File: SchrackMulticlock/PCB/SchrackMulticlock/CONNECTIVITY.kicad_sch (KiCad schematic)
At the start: 24 parts, among them J1 TYPE-C-31-M-12 (USB C CONN), U7 USBLC6-2SC6

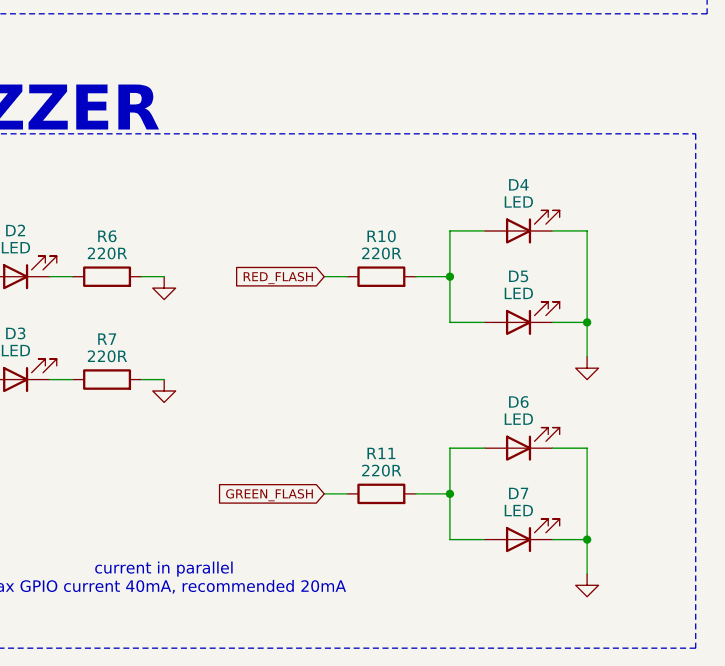
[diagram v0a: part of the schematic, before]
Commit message: Stopwatch.h + Schematic update
Multiclock Scheamtic and code update
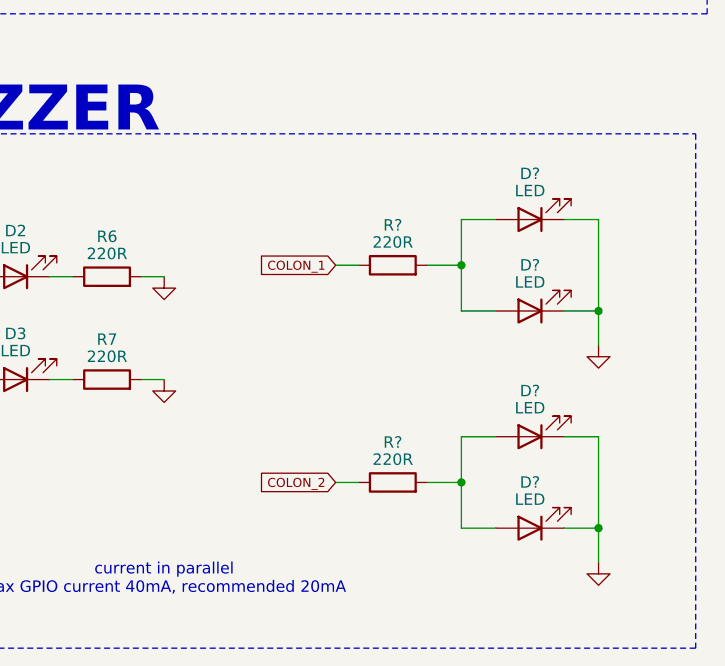
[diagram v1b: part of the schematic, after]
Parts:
- removed D4, D5, D6, D7: LED, LED_SMD:LED_0805_2012Metric_Pad1.15x1.40mm_HandSolder, symbol Device:LED
- removed R10, R11: 220R, Resistor_SMD:R_0805_2012Metric_Pad1.20x1.40mm_HandSolder, symbol Device:R
- added D? (x4): LED, LED_SMD:LED_0805_2012Metric_Pad1.15x1.40mm_HandSolder, symbol Device:LED
- added R? (x2): 220R, Resistor_SMD:R_0805_2012Metric_Pad1.20x1.40mm_HandSolder, symbol Device:R
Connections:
- net GND: now also D?.1 (K), D?.1 (K), D?.1 (K), D?.1 (K)
- new net: D?.2 (A), D?.2 (A), R?.2 (x2)
- new net COLON_1: R?.1
- new net COLON_2: R?.1

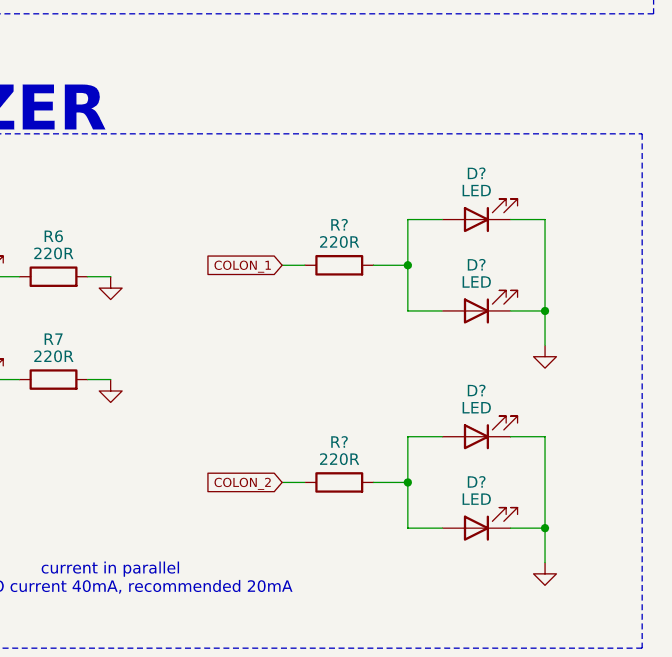
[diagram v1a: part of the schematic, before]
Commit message: SchrackMulticlock and Counter update
Schematic update for both
PCB update for Counter
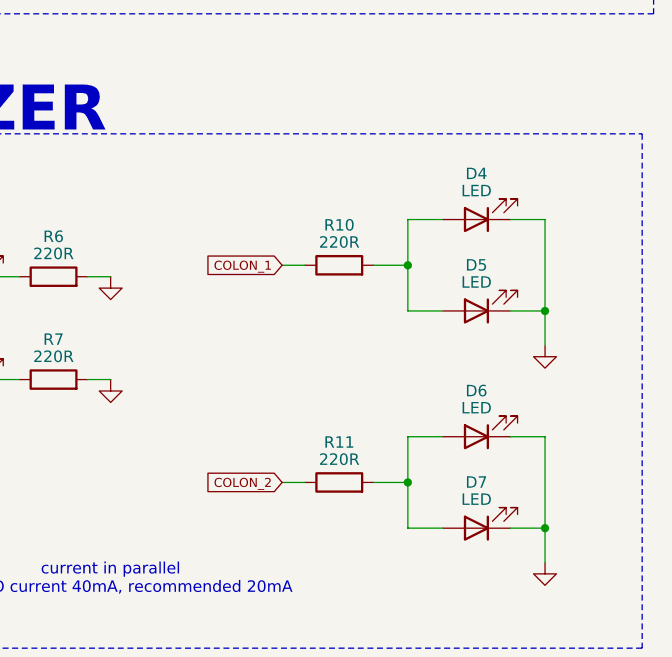
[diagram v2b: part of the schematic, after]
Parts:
- D4: renamed from D?; footprint LED_SMD:LED_0805_2012Metric_Pad1.15x1.40mm_HandSolder -> LED_SMD:LED_Cree-PLCC4_3.2x2.8mm_CCW
- gave numbers to parts that had none: 5
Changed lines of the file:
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@@
 		(on_board yes)
 		(dnp no)
-		(property "Reference" "D?"
+		(property "Reference" "D5"
 			(at 217.17 116.84 0)
 			(effects
@@
 			(project "SchrackMulticlock"
 				(path "/d96f2ffc-3f4c-4f71-b693-29f6b8c3245d/301b3ab9-8372-40d2-93c7-cd7607d23fc4"
-					(reference "D?")
+					(reference "D5")
 					(unit 1)
 				)
@@
 		(on_board yes)
 		(dnp no)
-		(property "Reference" "D?"
+		(property "Reference" "D6"
 			(at 217.17 130.81 0)
 			(effects
@@
 			(project "SchrackMulticlock"
 				(path "/d96f2ffc-3f4c-4f71-b693-29f6b8c3245d/301b3ab9-8372-40d2-93c7-cd7607d23fc4"
-					(reference "D?")
+					(reference "D6")
 					(unit 1)
 				)
@@
 		(dnp no)
 		(fields_autoplaced yes)
-		(property "Reference" "#PWR041"
+		(property "Reference" "#PWR023"
 			(at 224.79 132.08 0)
 			(effects
@@
 			(project "SchrackMulticlock"
 				(path "/d96f2ffc-3f4c-4f71-b693-29f6b8c3245d/301b3ab9-8372-40d2-93c7-cd7607d23fc4"
-					(reference "#PWR041")
+					(reference "#PWR023")
 					(unit 1)
 				)
@@
 		(dnp no)
 		(fields_autoplaced yes)
-		(property "Reference" "#PWR042"
+		(property "Reference" "#PWR024"
 			(at 224.79 156.21 0)
 			(effects
@@
 			(project "SchrackMulticlock"
 				(path "/d96f2ffc-3f4c-4f71-b693-29f6b8c3245d/301b3ab9-8372-40d2-93c7-cd7607d23fc4"
-					(reference "#PWR042")
+					(reference "#PWR024")
 					(unit 1)
 				)
@@
 		(on_board yes)
 		(dnp no)
-		(property "Reference" "R?"
+		(property "Reference" "R11"
 			(at 201.93 136.525 90)
 			(effects
@@
 			(project "SchrackMulticlock"
 				(path "/d96f2ffc-3f4c-4f71-b693-29f6b8c3245d/301b3ab9-8372-40d2-93c7-cd7607d23fc4"
-					(reference "R?")
+					(reference "R11")
 					(unit 1)
 				)
@@
 		(on_board yes)
 		(dnp no)
-		(property "Reference" "D?"
+		(property "Reference" "D7"
 			(at 217.17 140.97 0)
 			(effects
@@
 			(project "SchrackMulticlock"
 				(path "/d96f2ffc-3f4c-4f71-b693-29f6b8c3245d/301b3ab9-8372-40d2-93c7-cd7607d23fc4"
-					(reference "D?")
+					(reference "D7")
 					(unit 1)
 				)
@@
 		(on_board yes)
 		(dnp no)
-		(property "Reference" "R?"
+		(property "Reference" "R10"
 			(at 201.93 112.395 90)
 			(effects
@@
 			(project "SchrackMulticlock"
 				(path "/d96f2ffc-3f4c-4f71-b693-29f6b8c3245d/301b3ab9-8372-40d2-93c7-cd7607d23fc4"
-					(reference "R?")
+					(reference "R10")
 					(unit 1)
 				)
@@
 		(on_board yes)
 		(dnp no)
-		(property "Reference" "D?"
+		(property "Reference" "D4"
 			(at 217.17 106.68 0)
 			(effects
@@
 			)
 		)
-		(property "Footprint" "LED_SMD:LED_0805_2012Metric_Pad1.15x1.40mm_HandSolder"
+		(property "Footprint" "LED_SMD:LED_Cree-PLCC4_3.2x2.8mm_CCW"
 			(at 217.17 111.76 0)
 			(effects
@@
 			(project "SchrackMulticlock"
 				(path "/d96f2ffc-3f4c-4f71-b693-29f6b8c3245d/301b3ab9-8372-40d2-93c7-cd7607d23fc4"
-					(reference "D?")
-					(unit 1)
-				)
+					(reference "D4")
+					(unit 1)
+				)

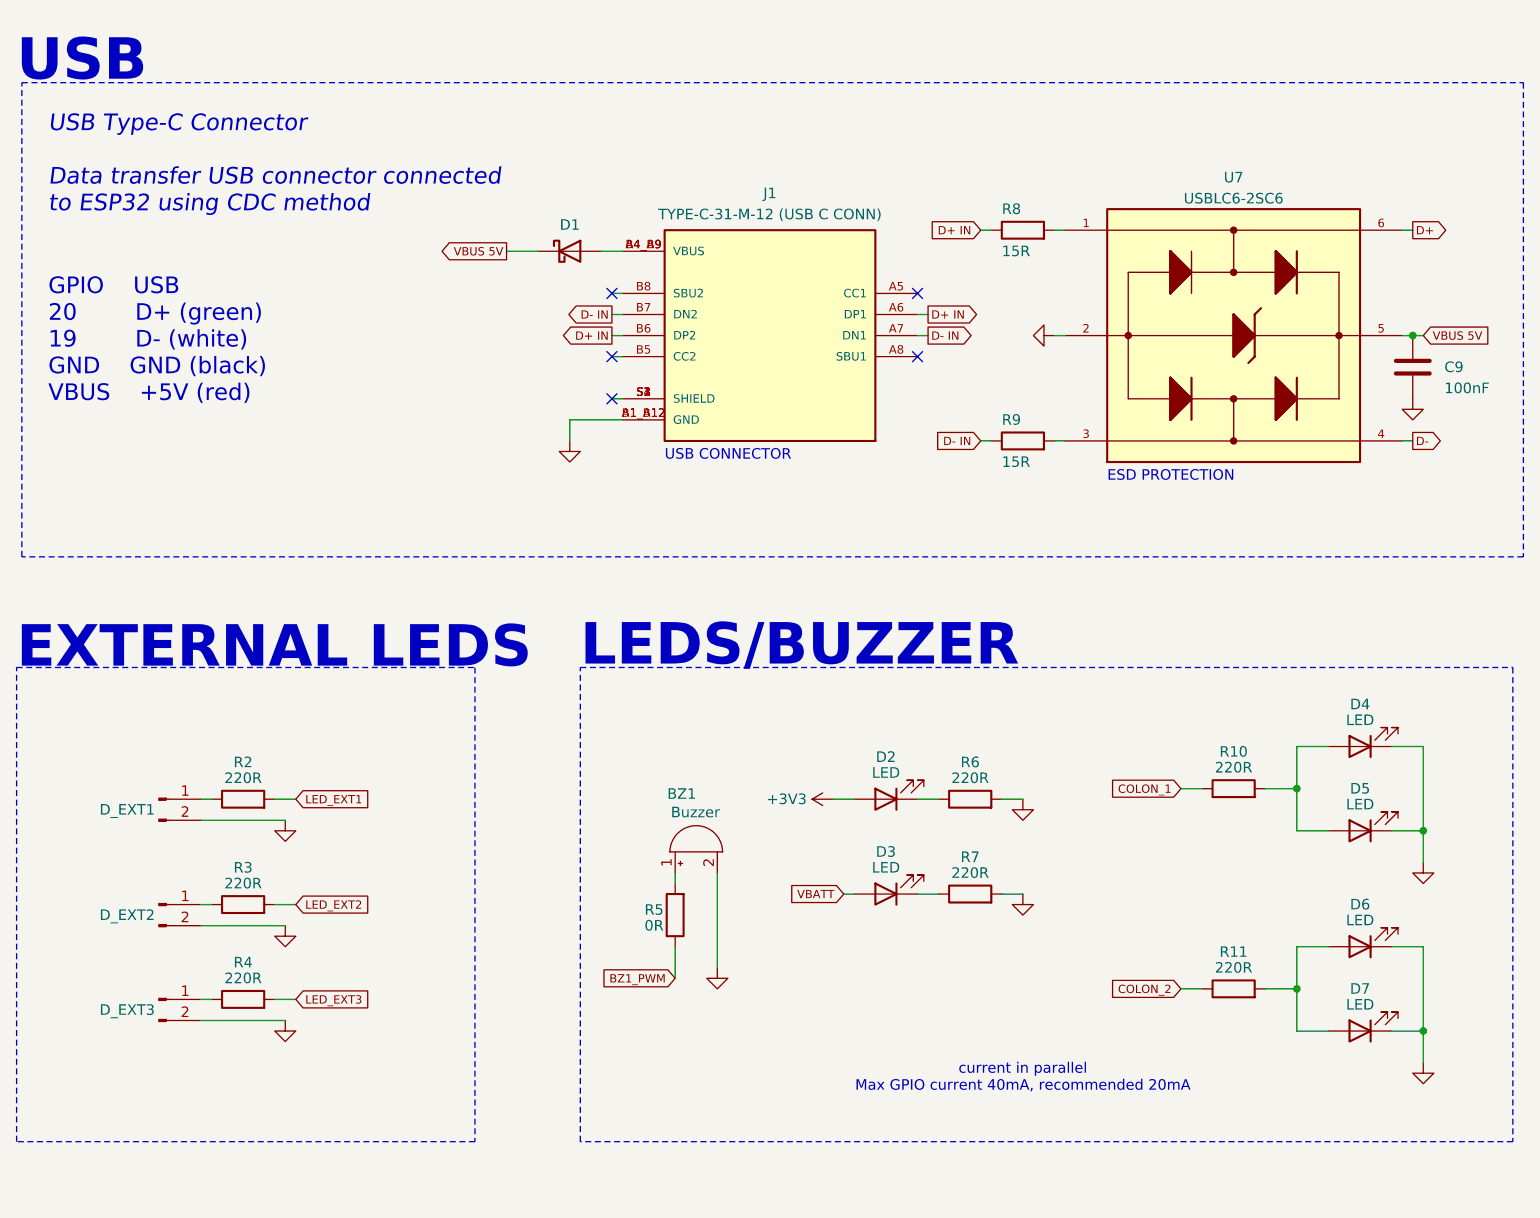
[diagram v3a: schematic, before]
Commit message: Schrackcounter Prototype update
Schematic + PCB update, final version
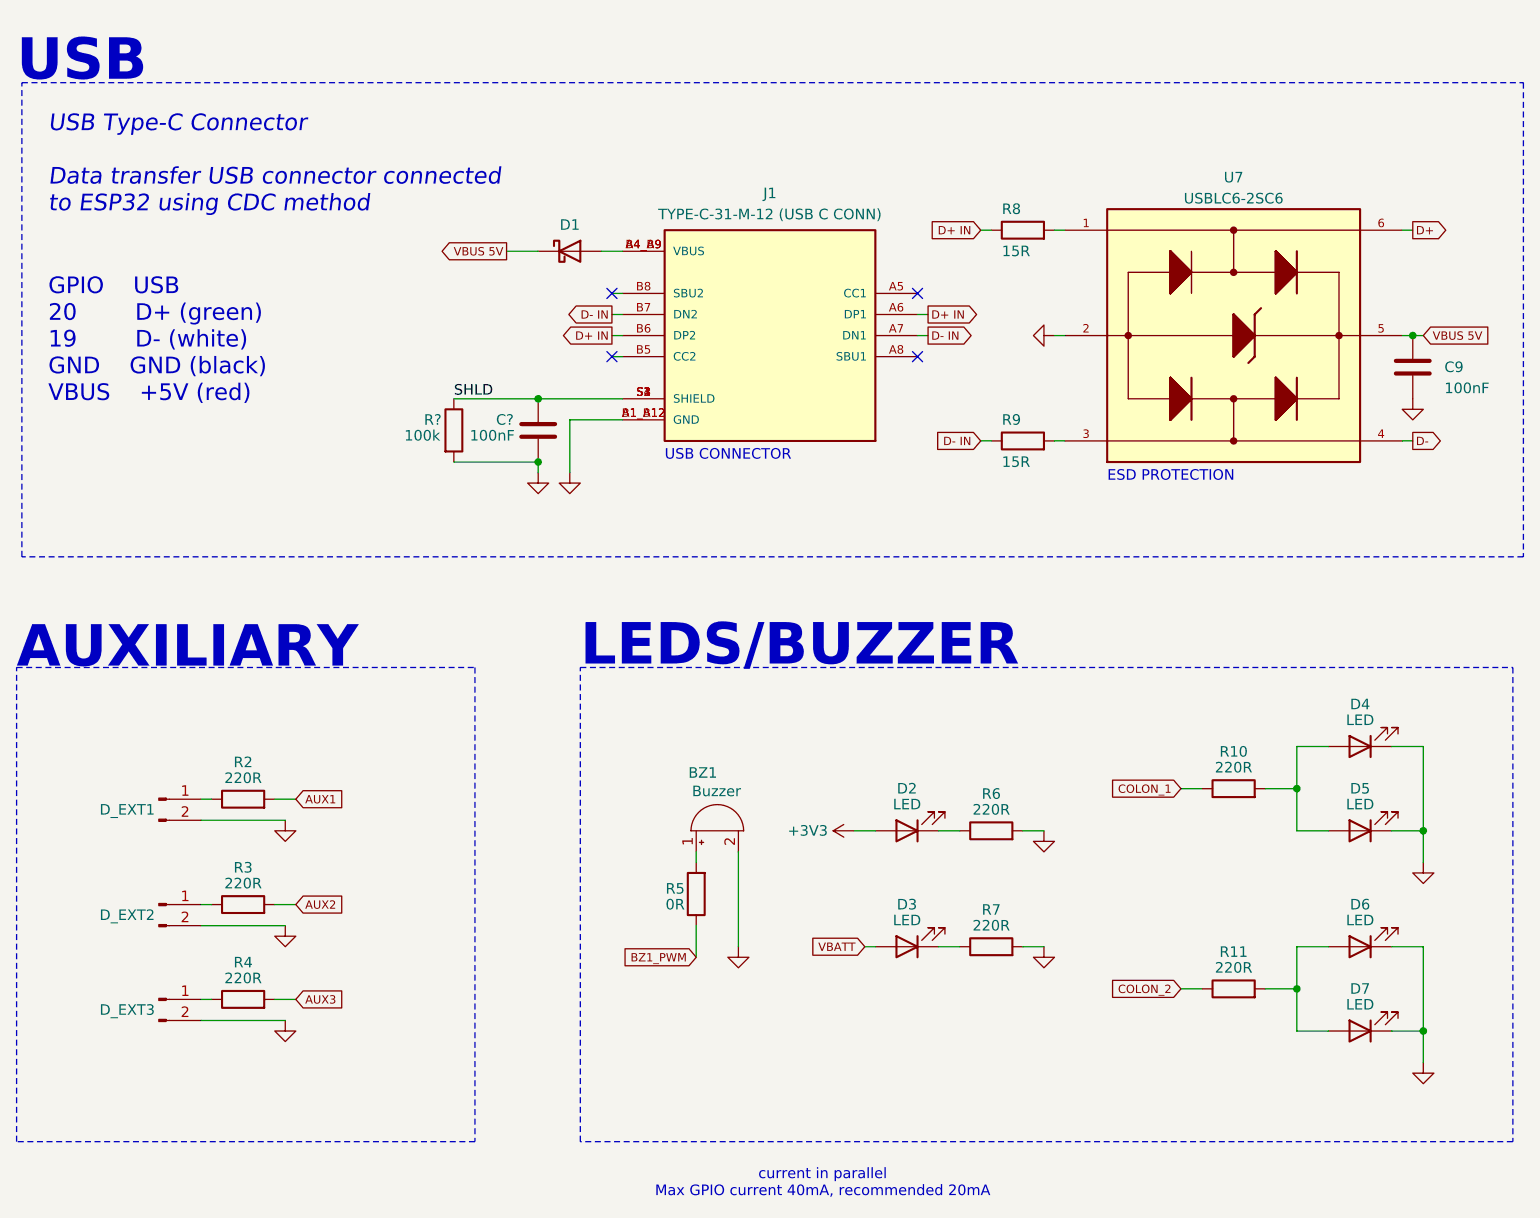
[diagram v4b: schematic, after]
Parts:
- added C?: 100nF, Capacitor_SMD:C_0805_2012Metric_Pad1.18x1.45mm_HandSolder, symbol Device:C
- added R?: 100k, Resistor_SMD:R_0805_2012Metric_Pad1.20x1.40mm_HandSolder, symbol Device:R
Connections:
- net GND: now also C?.1, R?.2
- net SHLD: now reaches J1.S1 (SHIELD), J1.S2 (SHIELD), J1.S3 (SHIELD), J1.S4 (SHIELD)
- net SHLD: now also C?.2, R?.1
- net LED_EXT1 renamed AUX1
- net LED_EXT2 renamed AUX2
- net LED_EXT3 renamed AUX3
- no-connect marks 5 -> 4
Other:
- note added: "AUXILIARY"
- note removed: "EXTERNAL LEDS"
- moved on the sheet: BZ1, D2, D3, R5, R6, R7
